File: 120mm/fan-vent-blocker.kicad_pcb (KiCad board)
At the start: 2 copper layers, 120 x 120 mm, 6 parts

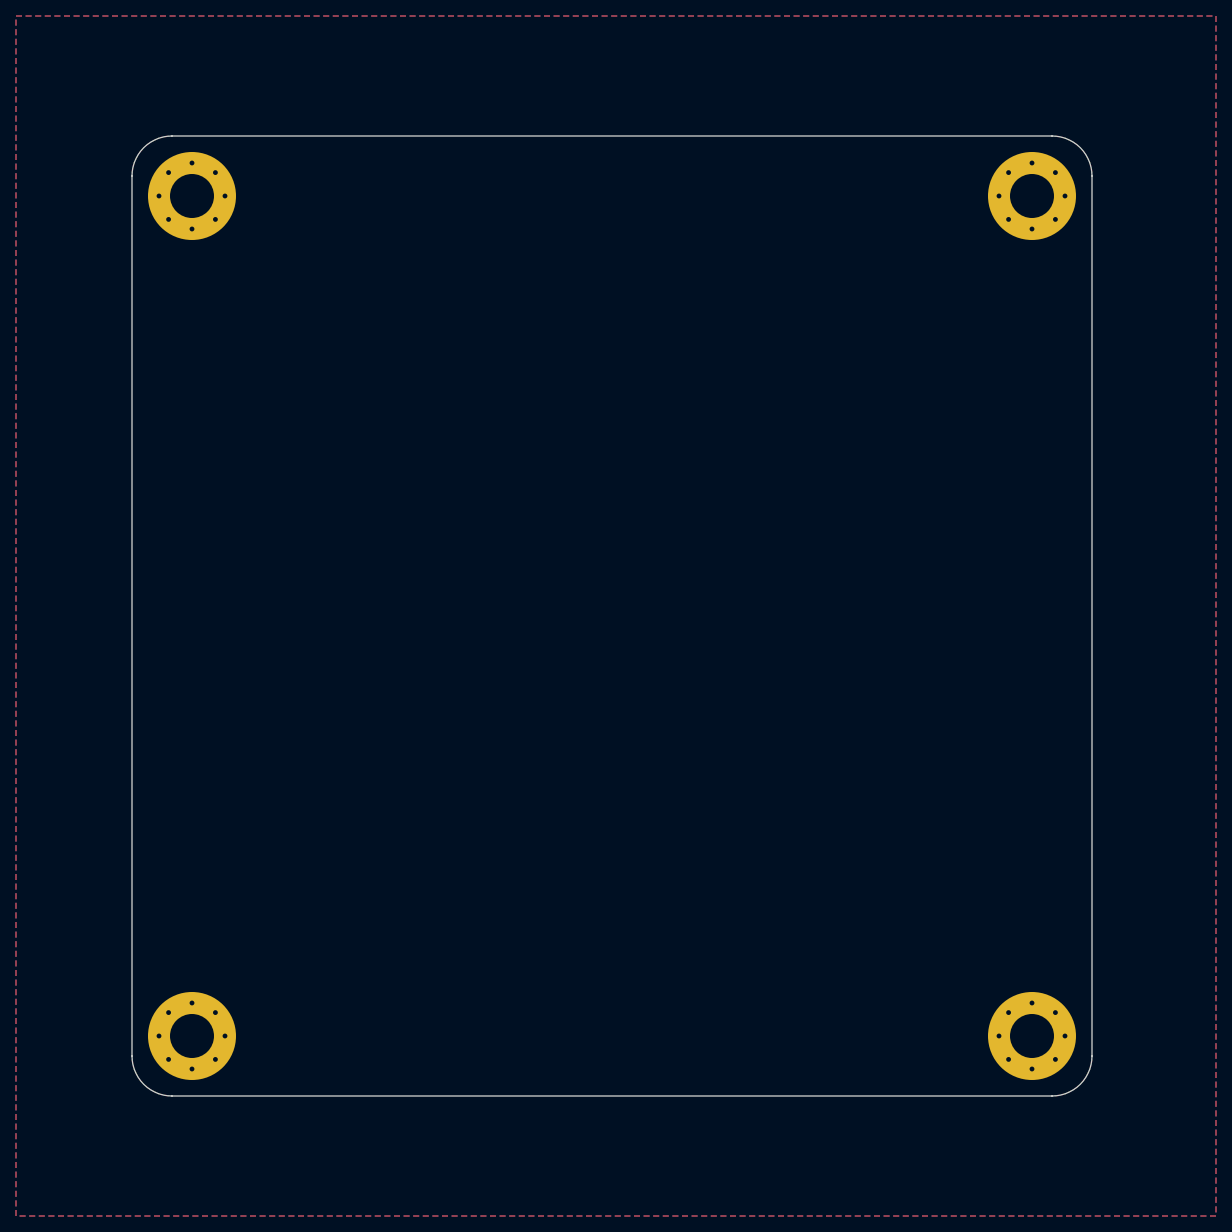
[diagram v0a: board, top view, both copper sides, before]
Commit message: Update to M4 mounting hardware
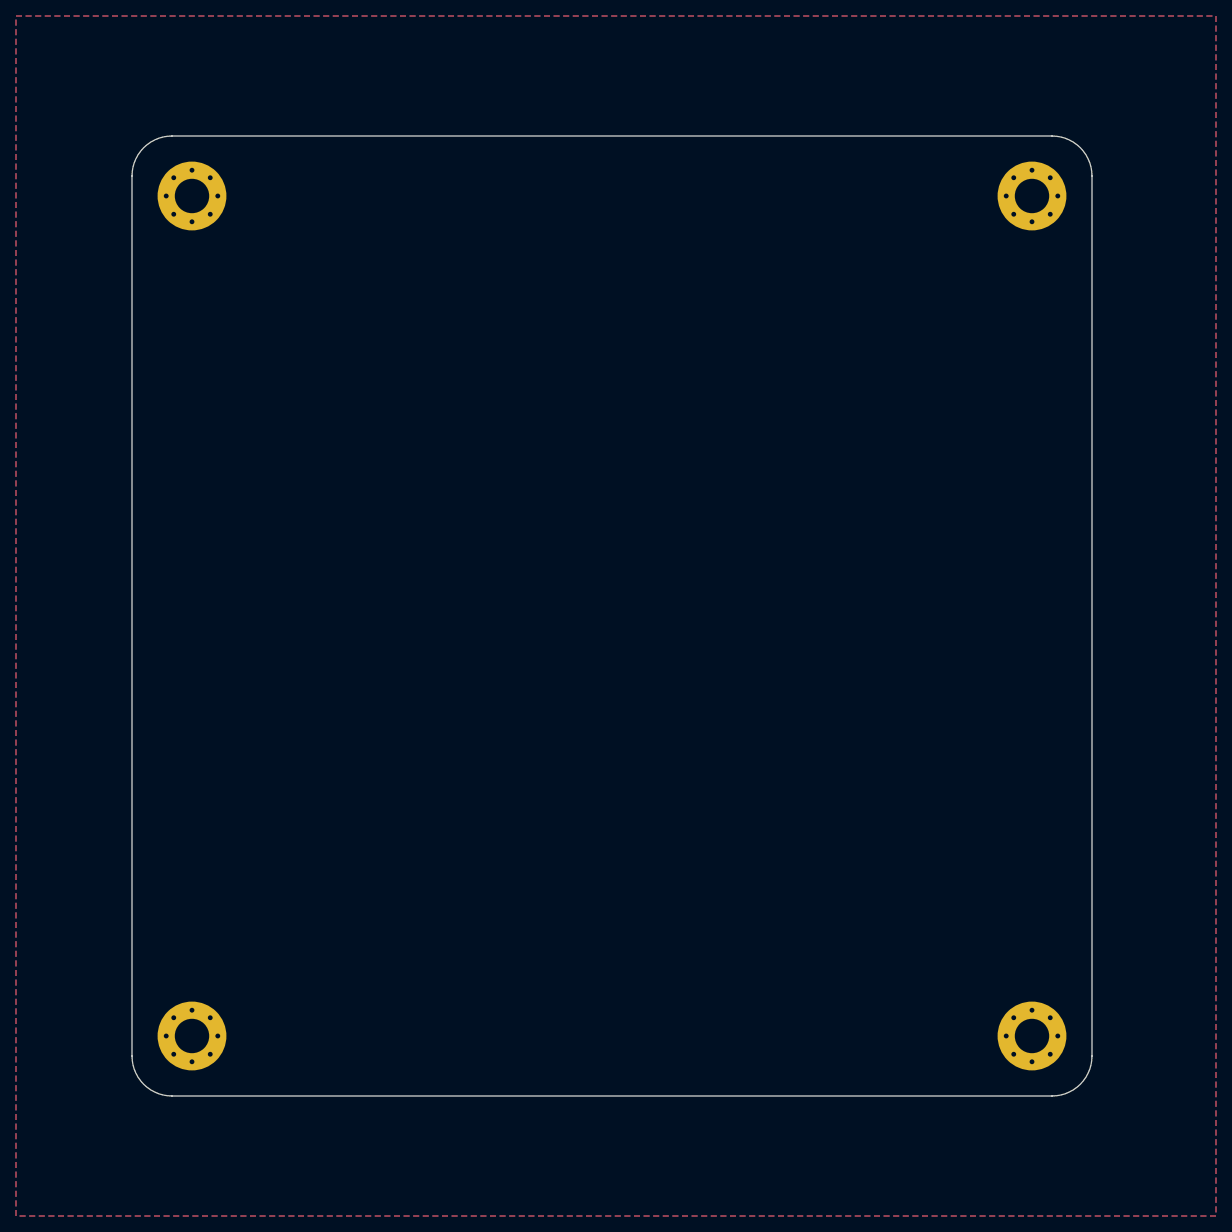
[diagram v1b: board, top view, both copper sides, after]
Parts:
- removed the G*** at (-44.0, 44.0)
- MH1, MH2, MH3, MH4: footprint locallib:MountingHole_5.5mm_Pad_Via -> MountingHole:MountingHole_4.3mm_M4_Pad_Via
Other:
- board text added: "120mm Fan Vent Blocker | www.ai03.com"
- board text removed: "120mm Fan Vent Blocker | www.ai03.me"
